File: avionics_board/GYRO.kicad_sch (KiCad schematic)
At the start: 6 parts, among them U3 BMI270

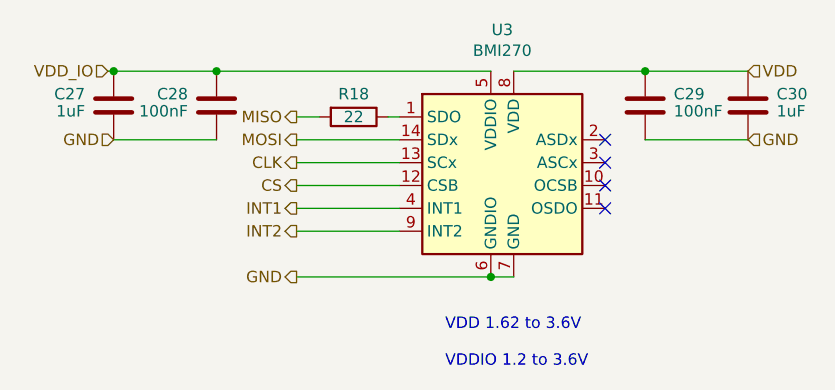
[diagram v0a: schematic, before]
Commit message: use SAMTEC connectors for AVI to side panels, try HARWIN ones next
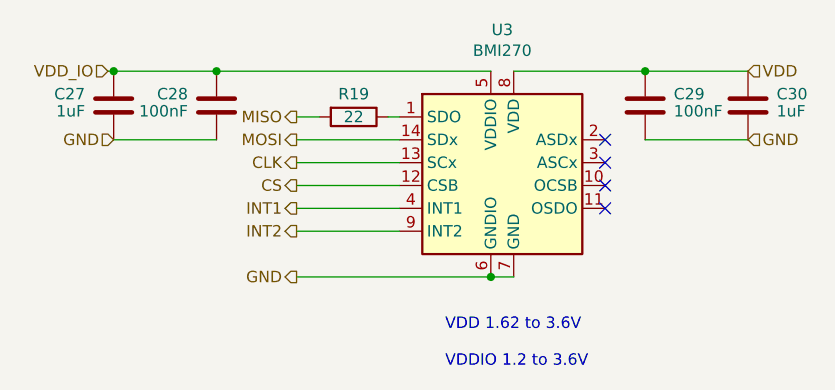
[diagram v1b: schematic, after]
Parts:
- renumbered R18 to R19
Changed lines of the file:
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@@
 		(on_board yes)
 		(dnp no)
-		(property "Reference" "R18"
+		(property "Reference" "R19"
 			(at 125.73 86.36 90)
 			(effects
@@
 			(project "AVIONICS_BOARD"
 				(path "/f6cc00ab-17f1-4973-862f-7ac95fe70668/c3f14e3e-486e-4feb-9ec8-af11b6b598f6"
-					(reference "R18")
+					(reference "R19")
 					(unit 1)
 				)

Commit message: AVI: using through hole M50 connectors for sun detectors and ACS
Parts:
- C27, C28, C29, C30: Order https://www.digikey.com/product-detail/en/samsung-electro-m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 -> (none)
- R19: Order https://www.digikey.com/product-detail/en/koa-speer-electro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 -> (none)
- U3: Order https://www.digikey.com/product-detail/en/bosch-sensortec/B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 -> (none)
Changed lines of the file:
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@@
-			)
-		)
-		(property "Order" "https://www.digikey.com/product-detail/en/samsung-electro-mechanics/CL10B104KA8NNNC/1276-1006-1-ND/3889092"
-			(at 169.545 87.63 0)
-			(effects
-				(font
-					(size 1.27 1.27)
-				)
-				(hide yes)
 			)
 		)
@@
 			)
 		)
-		(property "Order" "https://www.digikey.com/product-detail/en/bosch-sensortec/BMG250/828-1065-1-ND/6187900"
-			(at 143.51 93.98 0)
-			(effects
-				(font
-					(size 1.27 1.27)
-				)
-				(hide yes)
-			)
-		)
 		(property "Alt" ""
 			(at 143.51 93.98 0)
@@
 			)
 		)
-		(property "Order" "https://www.digikey.com/product-detail/en/samsung-electro-mechanics/CL10B104KA8NNNC/1276-1006-1-ND/3889092"
-			(at 158.115 87.63 0)
-			(effects
-				(font
-					(size 1.27 1.27)
-				)
-				(hide yes)
-			)
-		)
 		(property "Alt" ""
 			(at 158.115 87.63 0)
@@
 		)
 		(property "Description" ""
-			(at 125.73 88.9 0)
-			(effects
-				(font
-					(size 1.27 1.27)
-				)
-				(hide yes)
-			)
-		)
-		(property "Order" "https://www.digikey.com/product-detail/en/koa-speer-electronics-inc/RK73Z1JTTD/2019-RK73Z1JTTDCT-ND/9847522"
 			(at 125.73 88.9 0)
 			(effects
@@
 			)
 		)
-		(property "Order" "https://www.digikey.com/product-detail/en/samsung-electro-mechanics/CL10B104KA8NNNC/1276-1006-1-ND/3889092"
-			(at 110.49 87.63 0)
-			(effects
-				(font
-					(size 1.27 1.27)
-				)
-				(hide yes)
-			)
-		)
 		(property "Alt" ""
 			(at 110.49 87.63 0)
@@
 			(effects
 				(font
-					(size 1.27 1.27)
-				)
-				(hide yes)
-			)
-		)
-		(property "Order" "https://www.digikey.com/product-detail/en/samsung-electro-mechanics/CL10B104KA8NNNC/1276-1006-1-ND/3889092"
-			(at 99.06 87.63 0)
-			(effects
-				(font

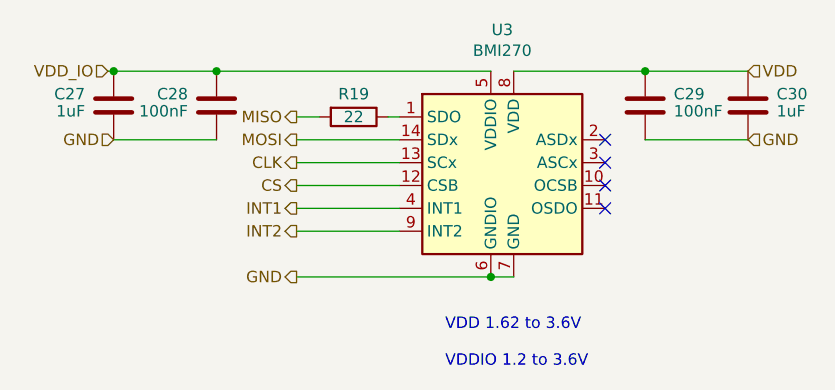
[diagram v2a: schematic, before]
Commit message: QC, add second 3V regulator to AUX, INT pullups on AUX SCI AVI
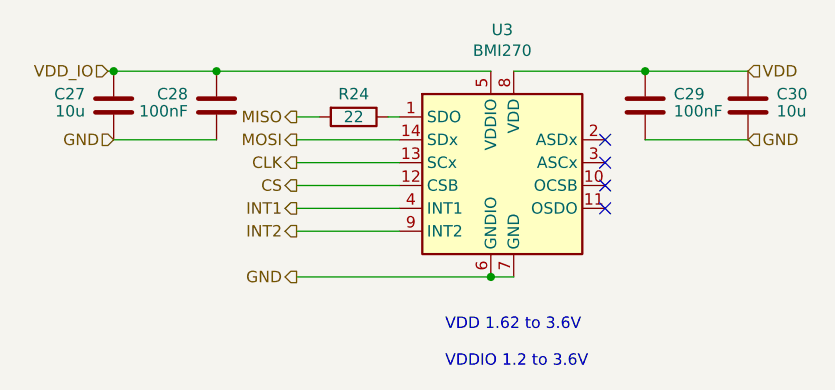
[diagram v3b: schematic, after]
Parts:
- C27, C30: value 1uF -> 10u; Part Number GRM188R61C105KA12D -> GRM188R61E106KA73D; Voltage 16 -> 25
- renumbered R19 to R24
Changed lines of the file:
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@@
 			)
 		)
-		(property "Value" "1uF"
+		(property "Value" "10u"
 			(at 172.72 88.265 0)
 			(effects
@@
 			)
 		)
-		(property "Datasheet" "https://search.murata.co.jp/Ceramy/image/img/A01X/G101/ENG/GRM188R61C105KA12-01.pdf"
+		(property "Datasheet" "https://search.murata.co.jp/Ceramy/image/img/A01X/G101/ENG/GRM188R61E106KA73-01.pdf"
 			(at 169.545 87.63 0)
 			(effects
@@
 			)
 		)
-		(property "Voltage" "16"
+		(property "Voltage" "25"
 			(at 174.625 90.17 0)
 			(effects
@@
 			)
 		)
-		(property "Part Number" "GRM188R61C105KA12D"
+		(property "Part Number" "GRM188R61E106KA73D"
 			(at 169.545 87.63 0)
 			(effects
@@
 		(on_board yes)
 		(dnp no)
-		(property "Reference" "R19"
+		(property "Reference" "R24"
 			(at 125.73 86.36 90)
 			(effects
@@
 			(project "AVIONICS_BOARD"
 				(path "/f6cc00ab-17f1-4973-862f-7ac95fe70668/c3f14e3e-486e-4feb-9ec8-af11b6b598f6"
-					(reference "R19")
+					(reference "R24")
 					(unit 1)
 				)
@@
 			)
 		)
-		(property "Value" "1uF"
+		(property "Value" "10u"
 			(at 95.885 88.265 0)
 			(effects
@@
 			)
 		)
-		(property "Datasheet" "https://search.murata.co.jp/Ceramy/image/img/A01X/G101/ENG/GRM188R61C105KA12-01.pdf"
+		(property "Datasheet" "https://search.murata.co.jp/Ceramy/image/img/A01X/G101/ENG/GRM188R61E106KA73-01.pdf"
 			(at 99.06 87.63 0)
 			(effects
@@
 			)
 		)
-		(property "Voltage" "16"
+		(property "Voltage" "25"
 			(at 93.98 90.17 0)
 			(effects
@@
 			)
 		)
-		(property "Part Number" "GRM188R61C105KA12D"
+		(property "Part Number" "GRM188R61E106KA73D"
 			(at 99.06 87.63 0)
 			(effects

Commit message: AVI board manages its local powers
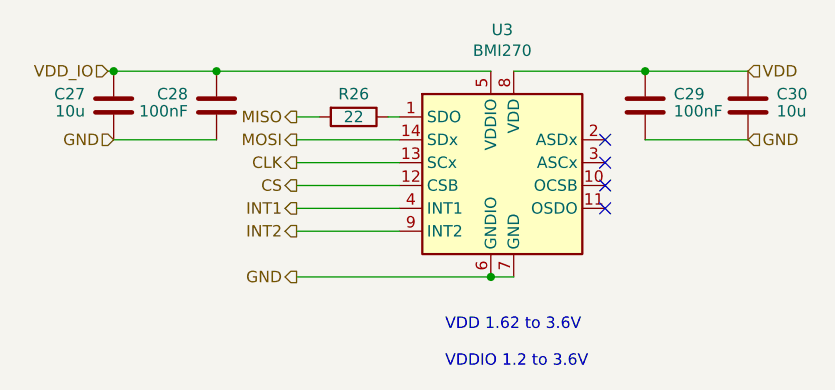
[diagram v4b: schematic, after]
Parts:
- renumbered R24 to R26
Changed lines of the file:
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@@
 		(on_board yes)
 		(dnp no)
-		(property "Reference" "R24"
+		(property "Reference" "R26"
 			(at 125.73 86.36 90)
 			(effects
@@
 			(project "AVIONICS_BOARD"
 				(path "/f6cc00ab-17f1-4973-862f-7ac95fe70668/c3f14e3e-486e-4feb-9ec8-af11b6b598f6"
-					(reference "R24")
+					(reference "R26")
 					(unit 1)
 				)
